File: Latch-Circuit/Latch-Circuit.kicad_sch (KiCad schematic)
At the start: 72 parts, among them J1 2-1445052-2, J2 3-794633-8, J3 B2P-VH, J4 3-794633-6, Q1 DMP3098LQ-7, Q2 2N7002K-AU_R1_000A2, Q3 2N7002K-AU_R1_000A2, Q4 2N7002K-AU_R1_000A2, Q5 2N7002K-AU_R1_000A2, Q6 2N7002K-AU_R1_000A2, Q7 2N7002K-AU_R1_000A2, U1 TLP3106A(TP,F, U2 TLP3106A(TP,F, U3 TLP3106A(TP,F, U4 CD4043BPWR

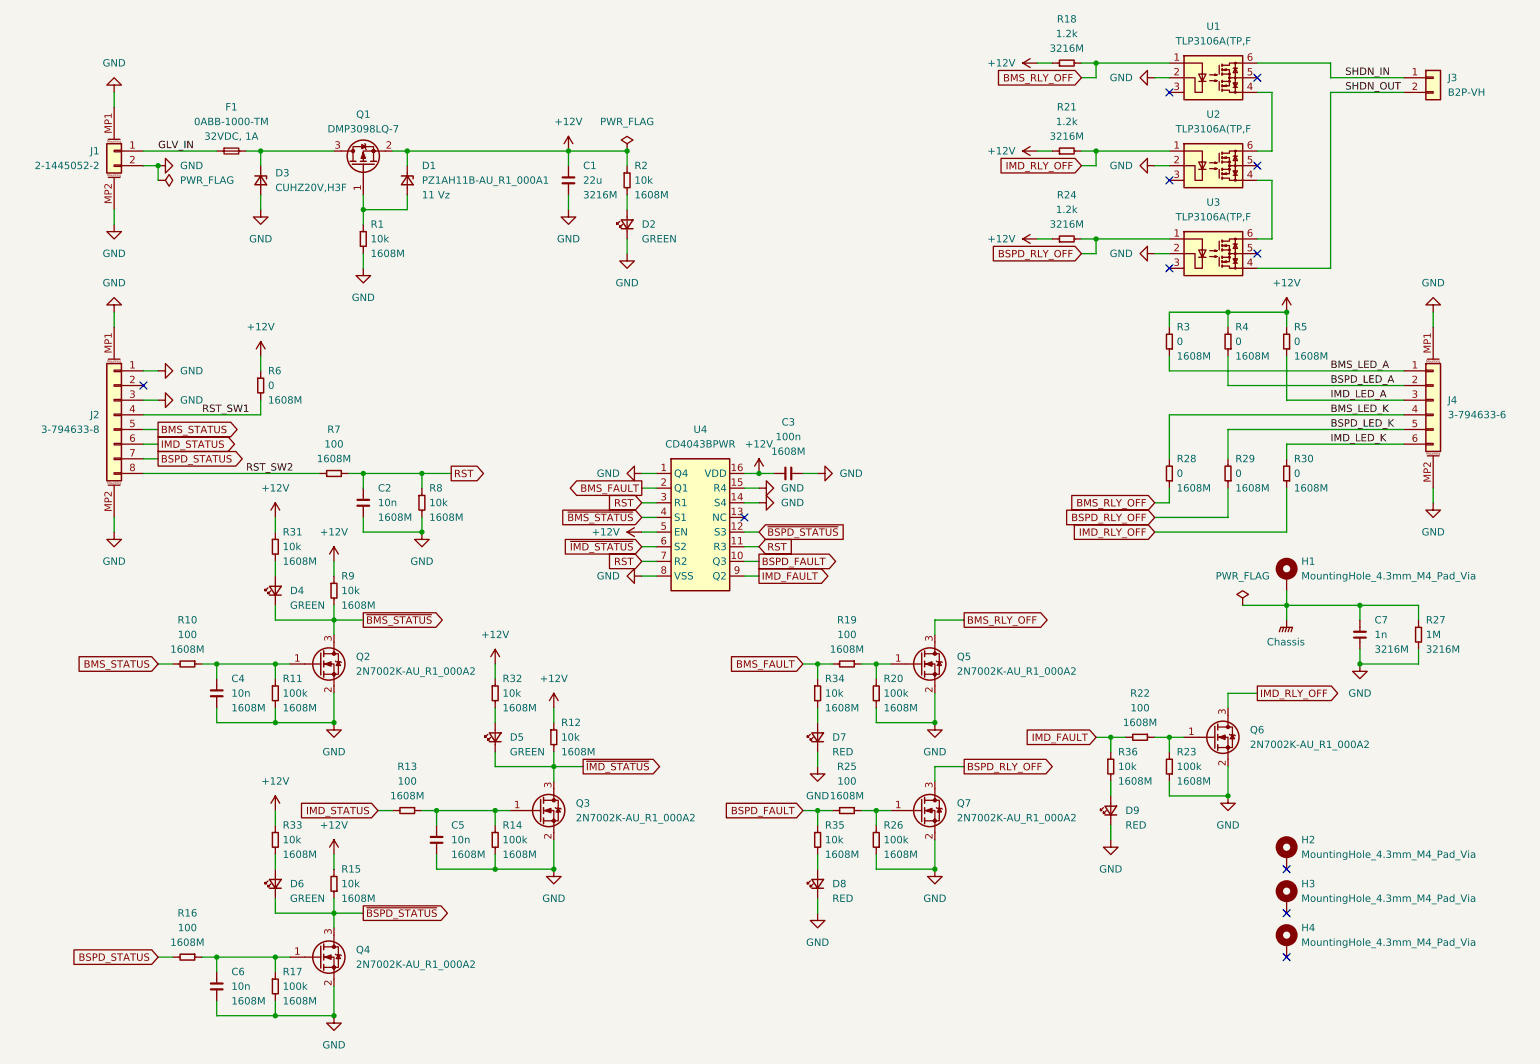
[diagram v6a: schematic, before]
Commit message: change relay and led drive circuit
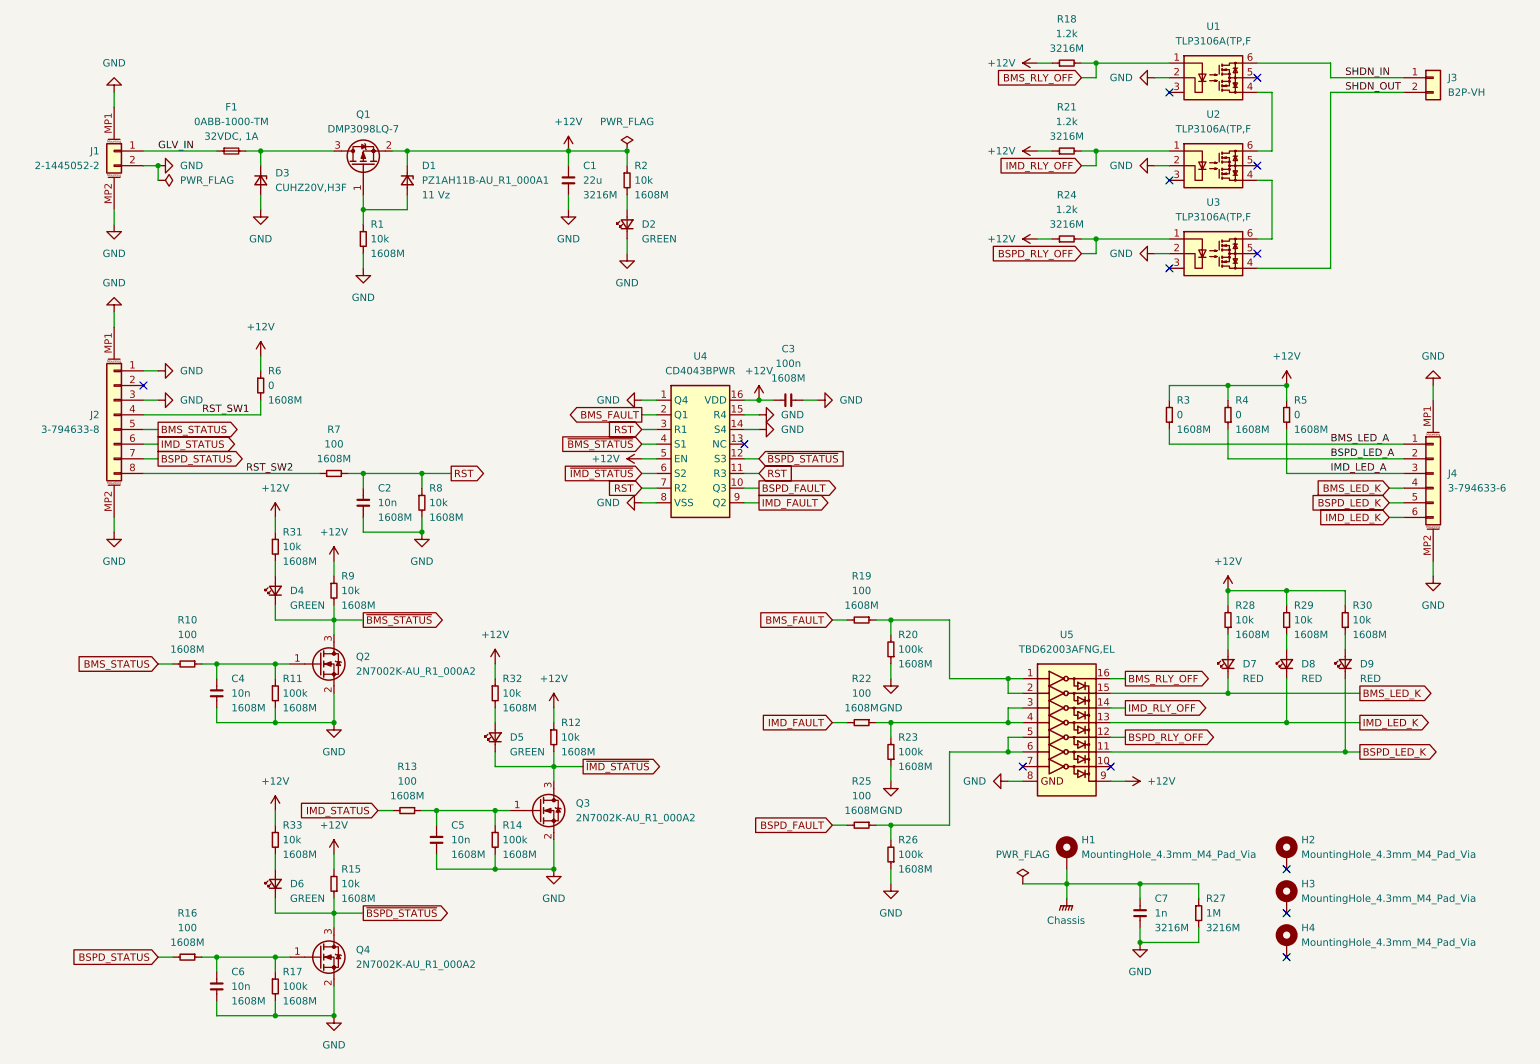
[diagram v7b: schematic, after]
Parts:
- removed Q5, Q6, Q7: 2N7002K-AU_R1_000A2, ProjectEV_Transistor:2N7002K-AU_R1_000A2, symbol ProjectEV_Transistor:2N7002K-AU_R1_000A2
- removed R34, R35, R36: 10k, ProjectEV_Resistor:R_1608M, symbol ProjectEV_Resistor:R_1608M
- added U5: TBD62003AFNG,EL, ProjectEV_PowerManagement:TBD62003AFNG,EL, symbol ProjectEV_PowerManagement:TBD62003AFNG,EL
- R28, R29, R30: value 0 -> 10k
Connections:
- net +12V: now also R28.2, R29.2, R30.2, U5.9 (COMMON)
- net BMS_LED_K: now also D7.1 (K), U5.15 (O2); no longer R28.2
- net BMS_RLY_OFF: now also U5.16 (O1); no longer R28.1
- net BSPD_LED_K: now also D9.1 (K), U5.11 (O6); no longer R29.2
- net BSPD_RLY_OFF: now also U5.12 (O5); no longer R29.1
- net GND: now also U5.8 (GND); no longer D7.1 (K), D8.1 (K), D9.1 (K)
- net IMD_LED_K: now also D8.1 (K), U5.13 (O4); no longer R30.2
- net IMD_RLY_OFF: now also U5.14 (O3); no longer R30.1
- net at D9.2 (A): now also R30.1
- net at R19.1, R20.2: now also U5.1 (I1), U5.2 (I2)
- net at R22.1, R23.2: now also U5.3 (I3), U5.4 (I4)
- net at D8.2 (A): now also R29.1
- net at R25.1, R26.2: now also U5.5 (I5), U5.6 (I6)
- net at D7.2 (A): now also R28.1
- no-connect marks 11 -> 13
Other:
- moved on the sheet: C3, C7, D7, D8, D9, H1, J4, R19, R20, R22, R23, R25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
